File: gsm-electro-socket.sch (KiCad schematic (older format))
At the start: 4 parts, among them U1 ArduinoProMini, U2 SIM800C

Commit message: update footprints
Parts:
- U2: footprint (none) -> boards:sim800c
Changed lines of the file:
@@
 F 0 "U2" H 3400 5400 60  0000 C CNN
 F 1 "SIM800C" H 3400 5500 60  0000 C CNN
-F 2 "" H 3400 5500 60  0001 C CNN
+F 2 "boards:sim800c" H 3400 5500 60  0001 C CNN
 F 3 "" H 3400 5500 60  0001 C CNN
 	1    2850 5050
@@
 $EndComp
 $Comp
-L GND #PWR4
+L GND #PWR01
 U 1 1 5A36E9AC
 P 6800 3250
-F 0 "#PWR4" H 6800 3000 50  0001 C CNN
+F 0 "#PWR01" H 6800 3000 50  0001 C CNN
 F 1 "GND" H 6800 3100 50  0000 C CNN
 F 2 "" H 6800 3250 50  0000 C CNN
@@
 $EndComp
 $Comp
-L GND #PWR1
+L GND #PWR02
 U 1 1 5A36EB91
 P 4400 4500
-F 0 "#PWR1" H 4400 4250 50  0001 C CNN
+F 0 "#PWR02" H 4400 4250 50  0001 C CNN
 F 1 "GND" H 4400 4350 50  0000 C CNN
 F 2 "" H 4400 4500 50  0000 C CNN
@@
 $EndComp
 $Comp
-L +5V #PWR5
+L +5V #PWR03
 U 1 1 5A36EBB7
 P 6800 3500
-F 0 "#PWR5" H 6800 3350 50  0001 C CNN
+F 0 "#PWR03" H 6800 3350 50  0001 C CNN
 F 1 "+5V" H 6800 3640 50  0000 C CNN
 F 2 "" H 6800 3500 50  0000 C CNN
@@
 $EndComp
 $Comp
-L +5V #PWR2
+L +5V #PWR04
 U 1 1 5A36EC33
 P 4500 4900
-F 0 "#PWR2" H 4500 4750 50  0001 C CNN
+F 0 "#PWR04" H 4500 4750 50  0001 C CNN
 F 1 "+5V" H 4500 5040 50  0000 C CNN
 F 2 "" H 4500 4900 50  0000 C CNN
@@
 Connection ~ 4800 3450
 $Comp
-L GND #PWR3
+L GND #PWR05
 U 1 1 5A36F0A7
 P 4800 3800
-F 0 "#PWR3" H 4800 3550 50  0001 C CNN
+F 0 "#PWR05" H 4800 3550 50  0001 C CNN
 F 1 "GND" H 4800 3650 50  0000 C CNN
 F 2 "" H 4800 3800 50  0000 C CNN
@@
 	4800 3150 5500 3150
 Wire Wire Line
-	4250 4600 5350 4600
+	4250 4600 5150 4600
 Wire Wire Line
-	5350 4600 5350 3250
+	5150 4600 5150 3250
 Wire Wire Line
-	5350 3250 5500 3250
+	5150 3250 5500 3250
 Wire Wire Line
 	4250 4700 4600 4700
@@
 Wire Wire Line
 	4600 3450 4800 3450
+$Comp
+L GND #PWR06
+U 1 1 5A3818A1
+P 6200 2800
+F 0 "#PWR06" H 6200 2550 50  0001 C CNN
+F 1 "GND" H 6200 2650 50  0000 C CNN
+F 2 "" H 6200 2800 50  0000 C CNN
+F 3 "" H 6200 2800 50  0000 C CNN
+	1    6200 2800
+	-1   0    0    1
+$EndComp
+$Comp
+L GND #PWR07
+U 1 1 5A38216C
+P 5500 3450
+F 0 "#PWR07" H 5500 3200 50  0001 C CNN
+F 1 "GND" H 5500 3300 50  0000 C CNN
+F 2 "" H 5500 3450 50  0000 C CNN
+F 3 "" H 5500 3450 50  0000 C CNN
+	1    5500 3450
+	0    1    1    0
+$EndComp
 $EndSCHEMATC

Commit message: change arduino to atmega328p
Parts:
- removed R1_100, R2_370: R_Small, Resistors_SMD:R_0402, symbol R_Small
- removed U1: ArduinoProMini, boards:ArduinoProMini, symbol ArduinoProMini
- added C1, C2: 22pF, Capacitors_SMD:C_0805_HandSoldering, symbol C
- added C3, C4: 0,1mF, Capacitors_SMD:C_0805_HandSoldering, symbol C
- added C5: 47mF, Capacitors_SMD:CP_Elec_8x10.5, symbol CP
- added IC1: ATMEGA328-P, Housings_QFP:TQFP-32_7x7mm_Pitch0.8mm, symbol ATMEGA328-P
- added Q1: BC337, TO_SOT_Packages_SMD:TSOT-23, symbol BC237
- added R1: 1k, Resistors_SMD:R_0805_HandSoldering, symbol R
- added R2: 10k, Resistors_SMD:R_0805_HandSoldering, symbol R
- added R3: 100k, Resistors_SMD:R_0805_HandSoldering, symbol R
- added R4: 47k, Resistors_SMD:R_0805_HandSoldering, symbol R
- added R5: 4.7k, Resistors_SMD:R_0805_HandSoldering, symbol R
- added R6: 370, Resistors_SMD:R_0805_HandSoldering, symbol R
- added R7: 100, Resistors_SMD:R_0805_HandSoldering, symbol R
- added SW1: RESET, Buttons_Switches_SMD:SW_DIP_x1_W5.08mm_Slide_Copal_CHS-A, symbol SW_PUSH_SMALL_H
- added Y1: 16Mhz, Crystals:Crystal_SMD_HC49-SD_HandSoldering, symbol Crystal
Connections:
- net labels added: MISO, MOSI, RST, SCK
- wire segments 15 -> 61
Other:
- note added: "R1 - 100\nR2 - 370\nR3 - 10k\nR4 - 47k\nR5 - 4,7k\nR6 - 1k\nR7 - 100k\n\nC1 - 22pF\nC2 - 22pF\nC3 - 47mF\nC4 - 0,1mF\nC5 - 0,1mF\n\nQ1 - BC337 (SMD)"

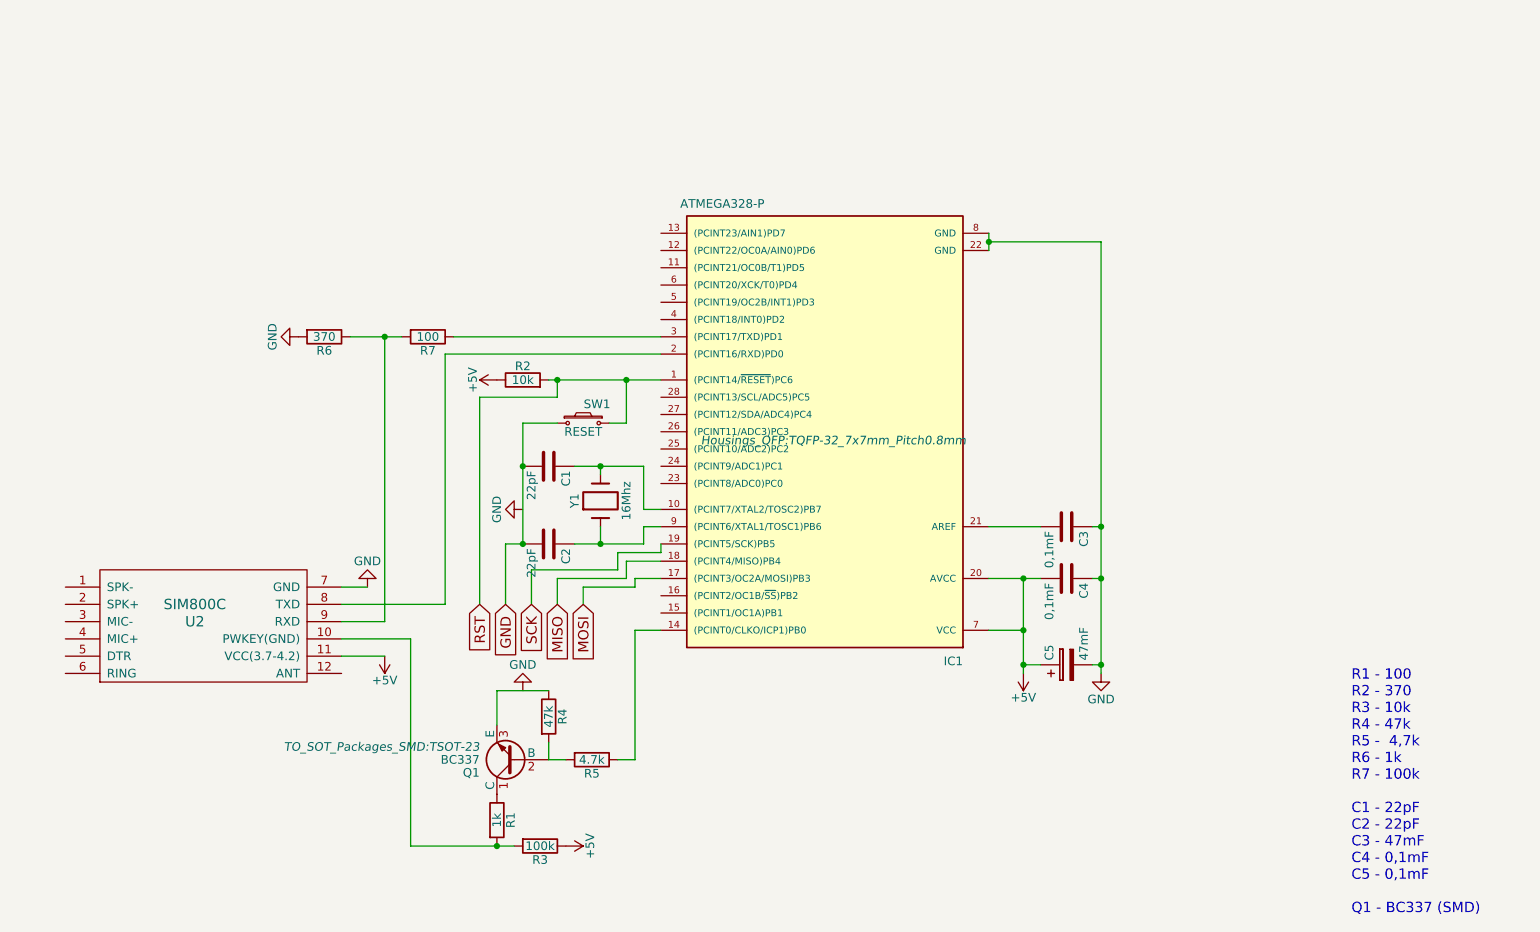
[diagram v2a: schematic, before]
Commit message: added power converter(step-down)
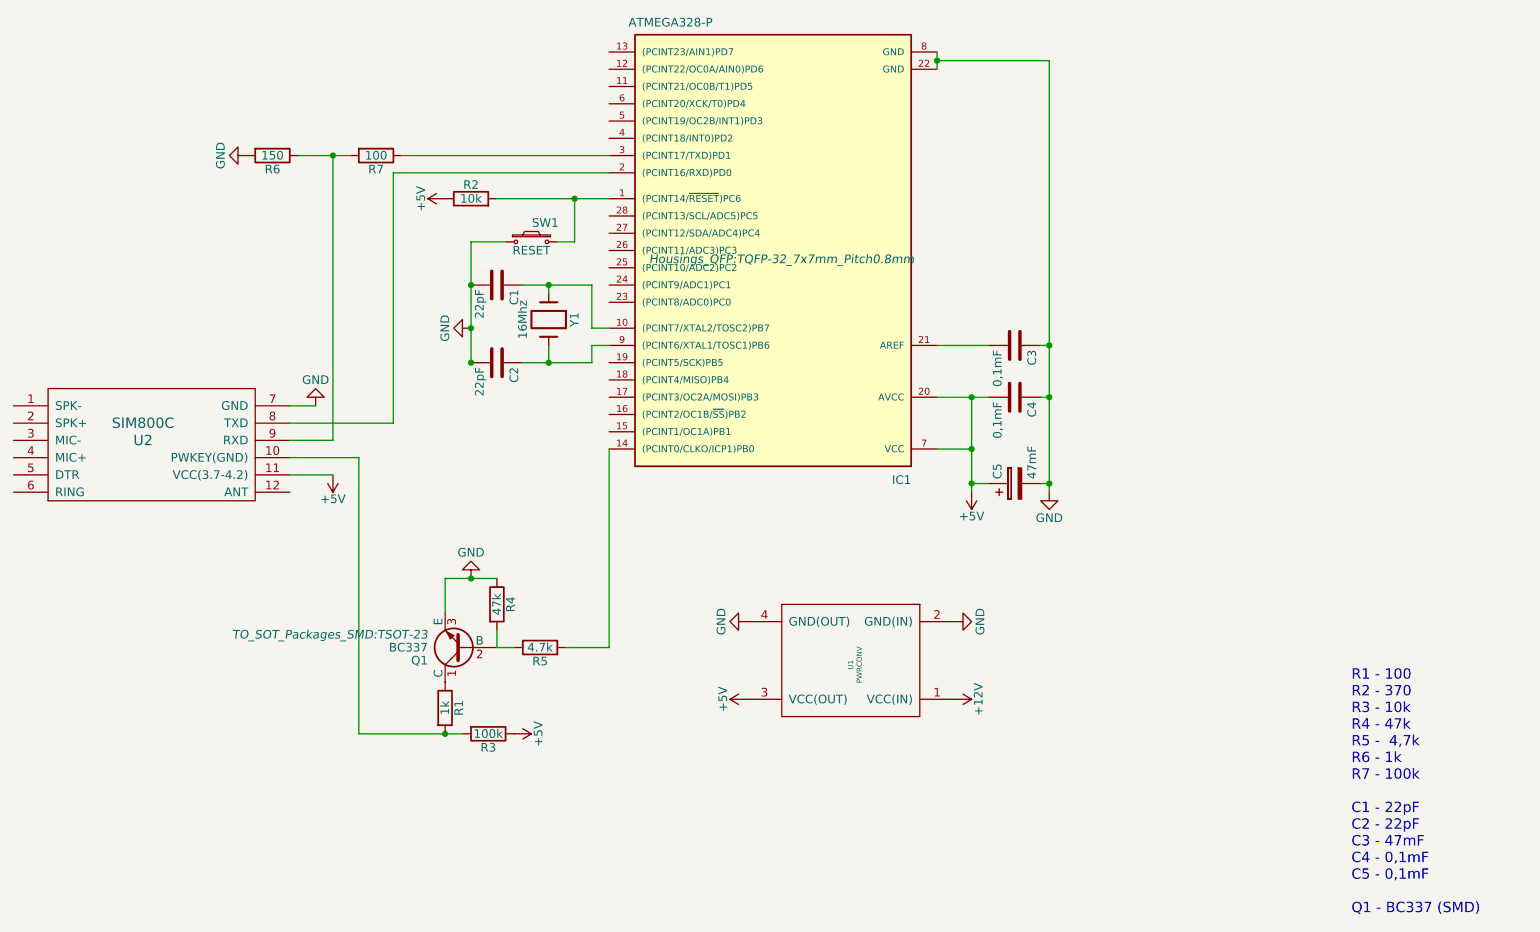
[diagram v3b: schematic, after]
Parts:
- added U1: PWRCONV, boards:PwrConvStepDown, symbol PWRCONV
- R6: value 370 -> 150
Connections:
- net +5V: now also U1.3 (VCC(OUT))
- net GND: now also Q1.3 (E), R4.1, U1.2 (GND(IN)), U1.4 (GND(OUT))
- net at C1.1, IC1.10 ((PCINT7/XTAL2/TOSC2)PB7): now also Y1.1; no longer Y1.2
- net at C2.1, IC1.9 ((PCINT6/XTAL1/TOSC1)PB6): now also Y1.2; no longer Y1.1
- net MISO: no longer names the net of IC1.18 ((PCINT4/MISO)PB4)
- net MOSI: no longer names the net of IC1.17 ((PCINT3/OC2A/MOSI)PB3)
- net RST: no longer names the net of IC1.1 ((PCINT14/~RESET~)PC6), R2.2, SW1.2
- net SCK: no longer names the net of IC1.19 ((PCINT5/SCK)PB5)
- new net +12V: U1.1 (VCC(IN))
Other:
- moved on the sheet: C1, C2, C3, C4, C5, IC1, Q1, R1, R2, R3, R4, R5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

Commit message: update schema
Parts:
- removed SW1: RESET, Buttons_Switches_SMD:SW_DIP_x1_W5.08mm_Slide_Copal_CHS-A, symbol SW_PUSH_SMALL_H
- added D1: LED, LEDs:LED_D2.0mm_W4.0mm_H2.8mm_FlatTop, symbol LED
- added P1, P2: CONN_01X03, Pin_Headers:Pin_Header_Angled_1x03_Pitch2.54mm, symbol CONN_01X03
- added R8: 1k, Resistors_SMD:R_0805_HandSoldering, symbol R
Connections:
- net +5V: now also P1.2 (P2)
- net GND: now also P1.1 (P1), R8.2
- net at IC1.1 ((PCINT14/~RESET~)PC6), R2.2: now also P1.3 (P3)
- net at IC1.17 ((PCINT3/OC2A/MOSI)PB3): now also P2.1 (P1)
- net at IC1.18 ((PCINT4/MISO)PB4): now also P2.2 (P2)
- net at IC1.19 ((PCINT5/SCK)PB5): now also P2.3 (P3)
- net at IC1.25 ((PCINT10/ADC2)PC2): now also D1.2 (A)
- new net: D1.1 (K), R8.1
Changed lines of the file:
@@
-$EndComp
-$Comp
-L SW_PUSH_SMALL_H SW1
-U 1 1 5A398B09
-P 5350 2500
-F 0 "SW1" H 5430 2610 50  0000 C CNN
-F 1 "RESET" H 5350 2450 50  0000 C CNN
-F 2 "Buttons_Switches_SMD:SW_DIP_x1_W5.08mm_Slide_Copal_CHS-A" H 5350 2700 50  0001 C CNN
-F 3 "" H 5350 2700 50  0000 C CNN
-	1    5350 2500
-	1    0    0    -1
 $EndComp
 $Comp
@@
 	5550 4850 5800 4850
 Wire Wire Line
-	5200 2500 5000 2500
-Wire Wire Line
-	5500 2500 5600 2500
-Wire Wire Line
-	5600 2500 5600 2250
-Connection ~ 5600 2250
-Wire Wire Line
 	5700 3200 5700 3100
 Wire Wire Line
@@
 Wire Wire Line
 	7900 3900 8000 3900
-Wire Wire Line
-	5000 2500 5000 3200
 $Comp
 L GND #PWR010
@@
 	0    1    1    0
 $EndComp
+$Comp
+L CONN_01X03 P2
+U 1 1 5A416111
+P 5250 3900
+F 0 "P2" H 5250 4100 50  0000 C CNN
+F 1 "CONN_01X03" V 5350 3900 50  0000 C CNN
+F 2 "Pin_Headers:Pin_Header_Angled_1x03_Pitch2.54mm" H 5250 3900 50  0001 C CNN
+F 3 "" H 5250 3900 50  0000 C CNN
+	1    5250 3900
+	0    1    1    0
+$EndComp
+Wire Wire Line
+	5150 3700 5150 3400
+Wire Wire Line
+	5150 3400 5650 3400
+Wire Wire Line
+	5650 3400 5650 3250
+Wire Wire Line
+	5650 3250 5750 3250
+Wire Wire Line
+	5750 3250 5750 3200
+Wire Wire Line
+	5750 3200 5800 3200
+Wire Wire Line
+	5800 3300 5700 3300
+Wire Wire Line
+	5700 3300 5700 3450
+Wire Wire Line
+	5700 3450 5250 3450
+Wire Wire Line
+	5250 3450 5250 3700
+Wire Wire Line
+	5350 3700 5350 3500
+Wire Wire Line
+	5350 3500 5750 3500
+Wire Wire Line
+	5750 3500 5750 3400
+Wire Wire Line
+	5750 3400 5800 3400
+Wire Wire Line
+	4650 2350 5200 2350
+Wire Wire Line
+	5200 2350 5200 2250
+Connection ~ 5200 2250
+Wire Wire Line
+	5000 3200 4850 3200
+Wire Wire Line
+	4850 3200 4850 3300
+$Comp
+L CONN_01X03 P1
+U 1 1 5A416B6A
+P 4750 3500
+F 0 "P1" H 4750 3700 50  0000 C CNN
+F 1 "CONN_01X03" V 4850 3500 50  0000 C CNN
+F 2 "Pin_Headers:Pin_Header_Angled_1x03_Pitch2.54mm" H 4750 3500 50  0001 C CNN
+F 3 "" H 4750 3500 50  0000 C CNN
+	1    4750 3500
+	0    1    1    0
+$EndComp
+Wire Wire Line
+	5000 2500 5000 3200
+Wire Wire Line
+	4650 3300 4650 2350
+$Comp
+L +5V #PWR014
+U 1 1 5A416D96
+P 4750 3300
+F 0 "#PWR014" H 4750 3150 50  0001 C CNN
+F 1 "+5V" H 4750 3440 50  0000 C CNN
+F 2 "" H 4750 3300 50  0000 C CNN
+F 3 "" H 4750 3300 50  0000 C CNN
+	1    4750 3300
+	1    0    0    -1
+$EndComp
+$Comp
+L R R8
+U 1 1 5A417393
+P 5150 2500
+F 0 "R8" V 5230 2500 50  0000 C CNN
+F 1 "1k" V 5150 2500 50  0000 C CNN
+F 2 "Resistors_SMD:R_0805_HandSoldering" V 5080 2500 50  0001 C CNN
+F 3 "" H 5150 2500 50  0000 C CNN
+	1    5150 2500
+	0    1    1    0
+$EndComp
+$Comp
+L LED D1
+U 1 1 5A4176DA
+P 5500 2500
+F 0 "D1" H 5500 2600 50  0000 C CNN
+F 1 "LED" H 5500 2400 50  0000 C CNN
+F 2 "LEDs:LED_D2.0mm_W4.0mm_H2.8mm_FlatTop" H 5500 2500 50  0001 C CNN
+F 3 "" H 5500 2500 50  0000 C CNN
+	1    5500 2500
+	1    0    0    -1
+$EndComp
+Wire Wire Line
+	5700 2500 5700 2650
+Wire Wire Line
+	5700 2650 5800 2650
 $EndSCHEMATC

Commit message: update pcb
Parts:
- removed IC1: ATMEGA328-P, Housings_QFP:TQFP-32_7x7mm_Pitch0.8mm, symbol ATMEGA328-P
- added IC1: ATMEGA328P-A, TQFP32, symbol ATMEGA328P-A
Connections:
- net +5V: now also P1.1 (P1), IC1.18 (AVCC), IC1.4 (VCC), IC1.6 (VCC); no longer P1.2 (P2)
- net GND: now also P1.2 (P2), IC1.21 (GND), IC1.3 (GND), IC1.5 (GND); no longer P1.1 (P1)
- net at U2.8 (TXD): now also IC1.30 ((PCINT16/RXD)PD0)
- net at P1.3 (P3), R2.2: now also IC1.29 ((PCINT14/~RESET~)PC6)
- net at C1.1, Y1.1: now also IC1.8 ((PCINT7/XTAL2/TOSC2)PB7)
- net at R5.1: now also IC1.14 ((PCINT2/OC1B/~SS~)PB2)
- net at P2.1 (P1): now also IC1.15 ((PCINT3/OC2A/MOSI)PB3)
- net at P2.2 (P2): now also IC1.16 ((PCINT4/MISO)PB4)
- net at P2.3 (P3): now also IC1.17 ((PCINT5/SCK)PB5)
- net at C3.2: now also IC1.20 (AREF)
- net at D1.2 (A): now also IC1.12 ((PCINT0/CLKO/ICP1)PB0)
- net at R7.1: now also IC1.31 ((PCINT17/TXD)PD1)
- net at C2.1, Y1.2: now also IC1.7 ((PCINT6/XTAL1/TOSC1)PB6)
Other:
- moved on the sheet: C1, C2, C3, C4, C5, D1, P1, P2, Q1, R1, R2, R3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

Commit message: update pcb
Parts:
- added P3: CONN_01X02, Pin_Headers:Pin_Header_Angled_1x02_Pitch2.54mm, symbol CONN_01X02
- added P4: CONN_01X03, Pin_Headers:Pin_Header_Angled_1x03_Pitch2.54mm, symbol CONN_01X03
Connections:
- net +5V: now also P4.1 (P1)
- net GND: now also P4.2 (P2); no longer U1.2 (GND(IN))
- net at IC1.1 ((PCINT19/OC2B/INT1)PD3): now also P4.3 (P3)
- net +12V: no longer names the net of U1.1 (VCC(IN))
- net +12V: now also P3.2 (P2)
- new net: P3.1 (P1), U1.2 (GND(IN))
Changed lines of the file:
@@
 $Comp
 L GND #PWR010
-U 1 1 5A3ECCE1
-P 7800 4700
-F 0 "#PWR010" H 7800 4450 50  0001 C CNN
-F 1 "GND" H 7800 4550 50  0000 C CNN
-F 2 "" H 7800 4700 50  0000 C CNN
-F 3 "" H 7800 4700 50  0000 C CNN
-	1    7800 4700
-	0    -1   -1   0
-$EndComp
-$Comp
-L +12V #PWR011
-U 1 1 5A3ECD19
-P 7800 5150
-F 0 "#PWR011" H 7800 5000 50  0001 C CNN
-F 1 "+12V" H 7800 5290 50  0000 C CNN
-F 2 "" H 7800 5150 50  0000 C CNN
-F 3 "" H 7800 5150 50  0000 C CNN
-	1    7800 5150
-	0    1    1    0
-$EndComp
-$Comp
-L GND #PWR012
 U 1 1 5A3ECD51
 P 6600 4700
-F 0 "#PWR012" H 6600 4450 50  0001 C CNN
+F 0 "#PWR010" H 6600 4450 50  0001 C CNN
 F 1 "GND" H 6600 4550 50  0000 C CNN
 F 2 "" H 6600 4700 50  0000 C CNN
@@
 $EndComp
 $Comp
-L +5V #PWR013
+L +5V #PWR011
 U 1 1 5A3ECD89
 P 6600 5150
-F 0 "#PWR013" H 6600 5000 50  0001 C CNN
+F 0 "#PWR011" H 6600 5000 50  0001 C CNN
 F 1 "+5V" H 6600 5290 50  0000 C CNN
 F 2 "" H 6600 5150 50  0000 C CNN
@@
 	4750 2650 4750 3850
 $Comp
-L +5V #PWR014
+L +5V #PWR012
 U 1 1 5A416D96
 P 4950 3850
-F 0 "#PWR014" H 4950 3700 50  0001 C CNN
+F 0 "#PWR012" H 4950 3700 50  0001 C CNN
 F 1 "+5V" H 4950 3990 50  0000 C CNN
 F 2 "" H 4950 3850 50  0000 C CNN
@@
 	5100 3500 5100 3050
 $Comp
-L GND #PWR015
+L GND #PWR013
 U 1 1 5A42E6F7
 P 5900 4700
-F 0 "#PWR015" H 5900 4450 50  0001 C CNN
+F 0 "#PWR013" H 5900 4450 50  0001 C CNN
 F 1 "GND" H 5900 4550 50  0000 C CNN
 F 2 "" H 5900 4700 50  0000 C CNN
@@
 Wire Wire Line
 	4400 5850 4400 3750
+$Comp
+L CONN_01X02 P3
+U 1 1 5A47F1A2
+P 8300 4900
+F 0 "P3" H 8300 5050 50  0000 C CNN
+F 1 "CONN_01X02" V 8400 4900 50  0000 C CNN
+F 2 "Pin_Headers:Pin_Header_Angled_1x02_Pitch2.54mm" H 8300 4900 50  0001 C CNN
+F 3 "" H 8300 4900 50  0000 C CNN
+	1    8300 4900
+	1    0    0    -1
+$EndComp
+Wire Wire Line
+	7800 4700 8100 4700
+Wire Wire Line
+	8100 4700 8100 4850
+Wire Wire Line
+	7800 5150 8100 5150
+Wire Wire Line
+	8100 5150 8100 4950
+$Comp
+L CONN_01X03 P4
+U 1 1 5A47FC07
+P 5000 1850
+F 0 "P4" H 5000 2050 50  0000 C CNN
+F 1 "CONN_01X03" V 5100 1850 50  0000 C CNN
+F 2 "Pin_Headers:Pin_Header_Angled_1x03_Pitch2.54mm" H 5000 1850 50  0001 C CNN
+F 3 "" H 5000 1850 50  0000 C CNN
+	1    5000 1850
+	-1   0    0    1
+$EndComp
+$Comp
+L GND #PWR014
+U 1 1 5A47FD81
+P 5200 1850
+F 0 "#PWR014" H 5200 1600 50  0001 C CNN
+F 1 "GND" H 5200 1700 50  0000 C CNN
+F 2 "" H 5200 1850 50  0000 C CNN
+F 3 "" H 5200 1850 50  0000 C CNN
+	1    5200 1850
+	0    -1   -1   0
+$EndComp
+$Comp
+L +5V #PWR015
+U 1 1 5A47FDC3
+P 5200 1950
+F 0 "#PWR015" H 5200 1800 50  0001 C CNN
+F 1 "+5V" H 5200 2090 50  0000 C CNN
+F 2 "" H 5200 1950 50  0000 C CNN
+F 3 "" H 5200 1950 50  0000 C CNN
+	1    5200 1950
+	-1   0    0    1
+$EndComp
+Wire Wire Line
+	5200 1750 5700 1750
+Wire Wire Line
+	5700 1750 5700 2100
+Wire Wire Line
+	5700 2100 5900 2100
 $EndSCHEMATC
